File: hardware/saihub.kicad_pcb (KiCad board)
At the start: 2 copper layers, 48 x 28 mm, 55 parts, among them J1 USB4105-GF-A, J2 1x12 2.54mm right-angle, Q1 AO3400A, SW1 BOOT, U1 USBLC6-2SC6, U2 SGM6232YPS8G/TR, U3 ESPC5-32E-H4, U4 TPS2553DBVR, U5 TPS2553DBVR

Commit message: feat(hardware): add header protection and refresh board deliverables
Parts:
- removed R13, R14: 10k, Saihub:R_0603_1608Metric
- added C21: 100n, Saihub:C_0603_1608Metric, F.Cu at (6.00, 4.30)
- added U10: USBLC6-2SC6, Saihub:SOT-23-6, F.Cu at (2.50, 5.50)
- added U6: TPD4E05U06DQAR, Saihub:TPD4E05U06_DQA, F.Cu at (14.5, 4.30)
- added U7: TPD4E05U06DQAR, Saihub:TPD4E05U06_DQA, F.Cu at (22.2, 4.30)
- D3: value SS14 -> SS34
- R10, R12, R9: value 100k -> 10k
- U4, U5: value TPS2553DBVR -> TPS2553DDBVR
- moved Q1 18.0 mm to (2.50, 25.5)
- moved R6 11.2 mm to (2.50, 15.8)
- moved C6 3.30 mm to (2.50, 8.80), turned to 0 degrees
- moved R11 2.36 mm to (15.3, 27.0)
- moved R12 2.05 mm to (22.0, 27.0), turned to 0 degrees
- moved U3 1.95 mm to (14.5, 15.6)
- moved TP3 1.90 mm to (5.60, 27.0)
- moved TP4 1.90 mm to (7.80, 27.0)
- moved TP5 1.90 mm to (10.0, 27.0)
- moved TP6 1.90 mm to (12.2, 27.0)
- moved C13 1.80 mm to (18.5, 27.0)
- moved C8 1.70 mm to (2.50, 14.1), turned to 0 degrees
- moved C7 1.70 mm to (2.50, 10.7), turned to 0 degrees
- moved TP1 0.80 mm to (1.20, 22.3)
- moved TP2 0.80 mm to (3.40, 22.3)
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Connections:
- U3 pad 19: unconnected-(U3-GPIO15-Pad19) -> FAULT4
- U3 pad 5: unconnected-(U3-GPIO3-Pad5) -> FAULT5
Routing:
- net GND: track 225.9 -> 8.61 mm, vias 12 -> 21
- net IO7: track 16.6 -> 42.6 mm, vias 1 -> 3
- net V3V3: track 137.6 -> 115.6 mm, vias 11 -> 13
- net IO3: track 15.1 -> 35.4 mm, vias 1 -> 4
- net FAULT4: track 41.4 -> 60.2 mm, vias 4 -> 6
- net V5: track 76.1 -> 93.4 mm, vias 8 -> 6
- net BUZZ_GATE: track 6.80 -> 23.5 mm, vias 0 -> 2
- net BUZZ_LOW: track 15.1 -> 31.4 mm
- net IO5: track 23.1 -> 38.7 mm, vias 1 -> 2
- net BUZZ_PWM: track 36.9 -> 21.9 mm, vias 4 -> 0
- net FAULT5: track 29.8 -> 43.0 mm, vias 2 -> 4
- net IO4: track 25.6 -> 35.3 mm, vias 1 -> 4
- net IO0: track 21.6 -> 30.8 mm, vias 1 -> 4
- net IO2: track 17.1 -> 25.6 mm, vias 1 -> 0
- net CC2: track 8.73 -> 16.9 mm, vias 2 -> 0
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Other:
- board text added: "SAIHub-Mini Rev A 2026-09-24"
- board text removed: "SAIHub-Mini Rev A 2026-09-18"

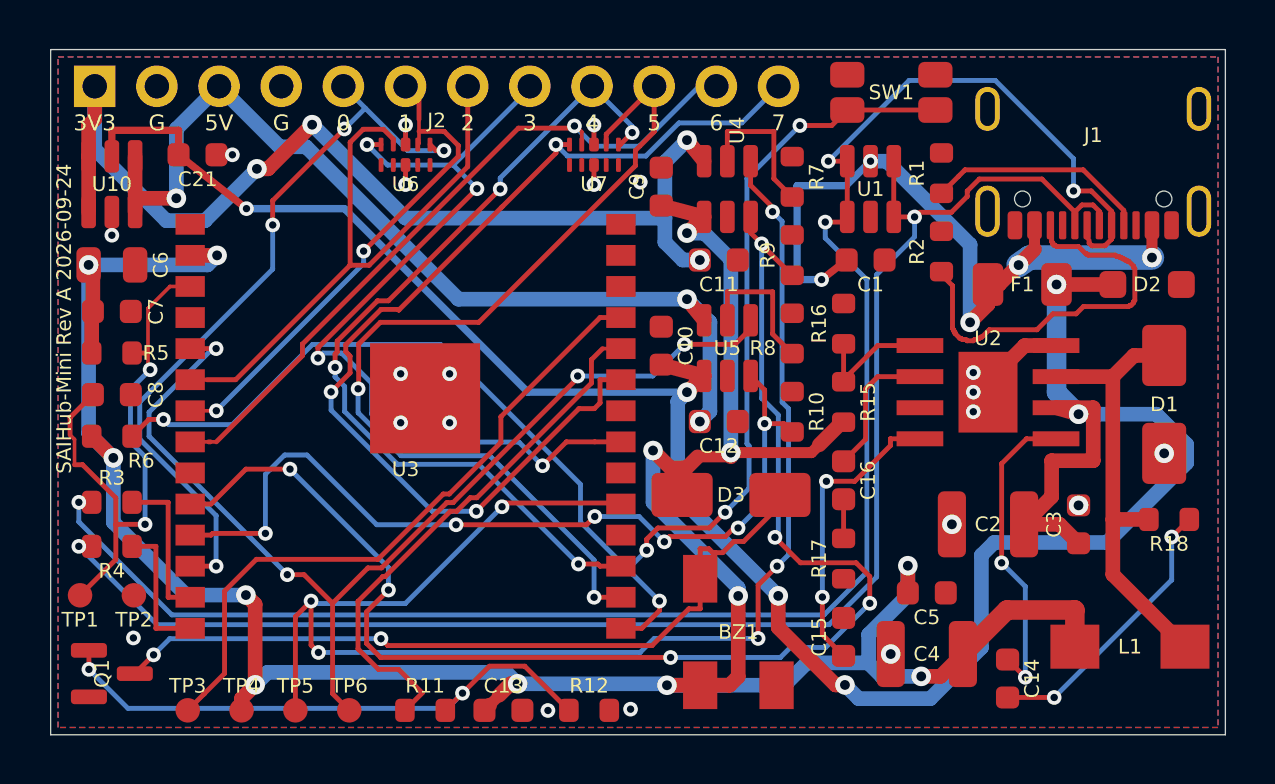
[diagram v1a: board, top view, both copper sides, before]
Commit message: Replace button and add corner antenna module without enlarging PCB
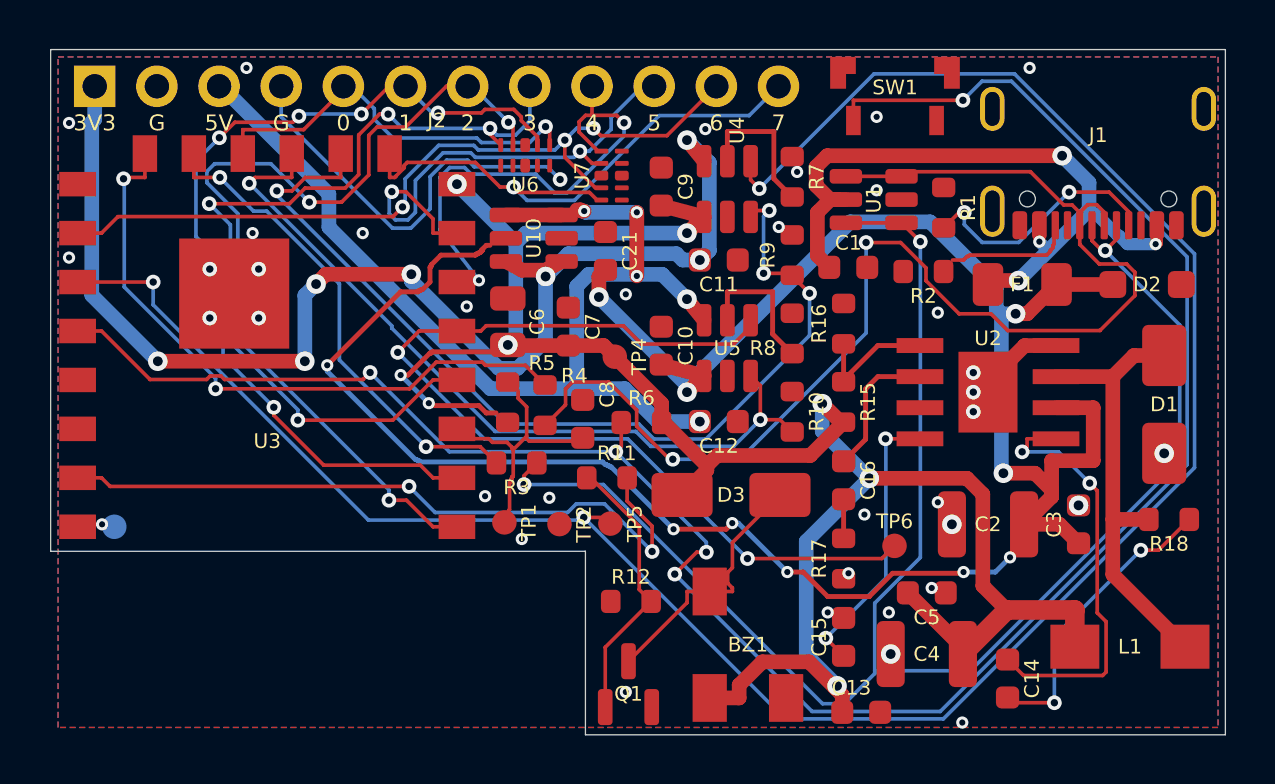
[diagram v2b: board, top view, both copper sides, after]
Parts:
- SW1: footprint Saihub:SW_SPST_EVQP7A -> Saihub:SW_SPST_TS2435VS
- TP3: moved to B.Cu
- U3: value ESPC5-32E-H4 -> ESPC5-12-H4; footprint Saihub:ESPC5-32E-H4 -> Saihub:ESPC5-12-H4
- moved TP6 23.3 mm to (34.5, 20.3)
- moved R6 21.6 mm to (24.1, 15.2), turned to 180 degrees
- moved Q1 21.1 mm to (23.6, 25.9), turned to 90 degrees
- moved TP4 21.0 mm to (23.1, 12.6)
- moved C8 19.3 mm to (21.7, 15.1), turned to 90 degrees
- moved C7 18.7 mm to (21.1, 11.3), turned to 90 degrees
- moved R4 18.6 mm to (20.2, 14.5), turned to 90 degrees
- moved TP2 17.6 mm to (20.8, 19.4)
- moved TP1 17.6 mm to (18.5, 19.3)
- moved U10 17.4 mm to (19.7, 7.71), turned to 180 degrees
- moved C21 17.1 mm to (22.7, 8.23), turned to 90 degrees
- moved R3 16.6 mm to (19.0, 16.9), turned to 180 degrees
- moved C6 16.3 mm to (18.7, 11.1), turned to 90 degrees
- moved R5 16.3 mm to (18.7, 14.4), turned to 90 degrees
- moved TP5 15.0 mm to (22.9, 19.4)
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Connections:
- U3 pad 1: GND -> IO2
- U3 pad 15: BOOT -> GND
- U3 pad 16: IO5 -> IO6
- U3 pad 17: IO4 -> FAULT4
- U3 pad 18: unconnected-(U3-GPIO27-Pad18) -> BOOT
- U3 pad 19: FAULT4 -> unconnected-(U3-GPIO27-Pad19)
- U3 pad 2: V3V3 -> IO1
- U3 pad 21: IO3 -> BUZZ_PWM
- U3 pad 22: unconnected-(U3-NC-Pad22) -> UART_TX
- U3 pad 23: IO7 -> GND
- U3 pad 4: unconnected-(U3-GPIO2-Pad4) -> IO3
- U3 pad 6: IO2 -> IO4
- U3 pad 7: IO1 -> IO5
- U3 pad 8: IO6 -> V3V3
- U3 pad 9: unconnected-(U3-GPIO7-Pad9) -> IO7
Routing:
- net FAULT4: track 60.2 -> 91.9 mm, vias 6 -> 3
- net BOOT: track 58.9 -> 86.7 mm
- net V3V3: track 115.6 -> 88.0 mm, vias 13 -> 8
- net UART_TX: track 26.9 -> 0.25 mm, vias 0 -> 1
- net BUZZ_LOW: track 31.4 -> 10.6 mm, vias 2 -> 0
- net MCU_DP: track 5.72 -> 26.3 mm, vias 0 -> 2
- net IO7: track 42.6 -> 23.6 mm, vias 3 -> 1
- net IO5: track 38.7 -> 20.1 mm
- net PWR3_EN: track 56.6 -> 39.1 mm, vias 6 -> 4
- net IO1: track 20.8 -> 36.9 mm, vias 2 -> 5
- net IO4: track 35.3 -> 20.4 mm, vias 4 -> 2
- net EN: track 23.5 -> 9.00 mm, vias 2 -> 0
- net IO0: track 30.8 -> 16.5 mm, vias 4 -> 1
- net MCU_DM: track 6.25 -> 20.0 mm, vias 0 -> 2
- net CC2: track 16.9 -> 4.71 mm
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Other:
- outline, holes or cut-outs redrawn

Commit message: feat(hardware): add grouped indicators and reproducible routing
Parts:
- added D4: GREEN, Saihub:LED_AA1608, F.Cu at (30.3, 5.20)
- added D5: GREEN, Saihub:LED_AA1608, F.Cu at (30.3, 8.40)
- added D6: RED, Saihub:LED_AA1608, F.Cu at (30.3, 11.6)
- added D7: BLUE, Saihub:LED_AA1608, F.Cu at (30.3, 14.8)
- added R19: 680, Saihub:R_0603_1608Metric, B.Cu at (32.1, 5.20)
- added R20: 1.5k, Saihub:R_0603_1608Metric, B.Cu at (29.2, 8.05)
- added R21: 1.5k, Saihub:R_0603_1608Metric, B.Cu at (32.0, 10.8)
- added R22: 330, Saihub:R_0603_1608Metric, B.Cu at (30.4, 16.6)
- R10, R7, R8, R9: moved to B.Cu
- moved R8 4.31 mm to (26.0, 11.2), turned to 0 degrees
- moved R10 4.00 mm to (34.2, 14.2)
- moved R9 3.96 mm to (34.1, 9.50)
- moved R7 2.47 mm to (28.0, 4.30)
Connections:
- U3 pad 20: unconnected-(U3-GPIO26-Pad20) -> STATUS_LED
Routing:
- net STATUS_LED: track 0.00 -> 32.8 mm, vias 0 -> 3
- net FAULT4: track 91.9 -> 59.3 mm
- net V3_SW: track 52.2 -> 60.4 mm, vias 7 -> 9
- net PWR5_EN: track 32.1 -> 39.9 mm, vias 2 -> 3
- net ILIM4: track 6.10 -> 0.00 mm, vias 0 -> 1
- net BUZZ_LOW: track 10.6 -> 6.37 mm
- net V5: track 94.1 -> 97.6 mm
- net V5_SW: track 43.9 -> 46.2 mm
- net PWR3_EN: track 39.1 -> 41.2 mm, vias 4 -> 5
- net D6_A: track 0.00 -> 1.21 mm, vias 0 -> 1
- net ILIM5: track 5.87 -> 4.74 mm, vias 0 -> 1
- net D4_A: track 0.00 -> 1.10 mm, vias 0 -> 1
- net GND: vias 37 -> 36
- net D7_A: vias 0 -> 1
- net D5_A: vias 0 -> 1

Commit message: fix(hardware): correct assembly footprints and package outlines
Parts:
- BZ1: value KLJ-5020 3.3V -> 5020 3V 4kHz; footprint Saihub:KLJ-5020 -> Saihub:Buzzer_5020_Supplied
- D4, D5, D6, D7: footprint Saihub:LED_AA1608 -> Saihub:LED_0603_1608Metric
- R19: value 680 -> 330
- R20: value 1.5k -> 1.2k
- SW1: footprint Saihub:SW_SPST_TS2435VS -> Saihub:SW_SPST_2X4_LocatingPins
- moved BZ1 0.50 mm to (28.5, 24.8), turned to 0 degrees
- turned D4 to -90 degrees
- turned D5 to -90 degrees
- turned D6 to -90 degrees
- turned D7 to 90 degrees
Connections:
- D4 pad 1: GND -> D4_A
- D4 pad 2: D4_A -> GND
- D5 pad 1: GND -> D5_A
- D5 pad 2: D5_A -> GND
- D6 pad 1: GND -> D6_A
- D6 pad 2: D6_A -> GND
- D7 pad 1: GND -> D7_A
- D7 pad 2: D7_A -> GND
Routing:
- net BUZZ_LOW: track 6.37 -> 11.7 mm
- net V3V3: track 88.0 -> 85.2 mm

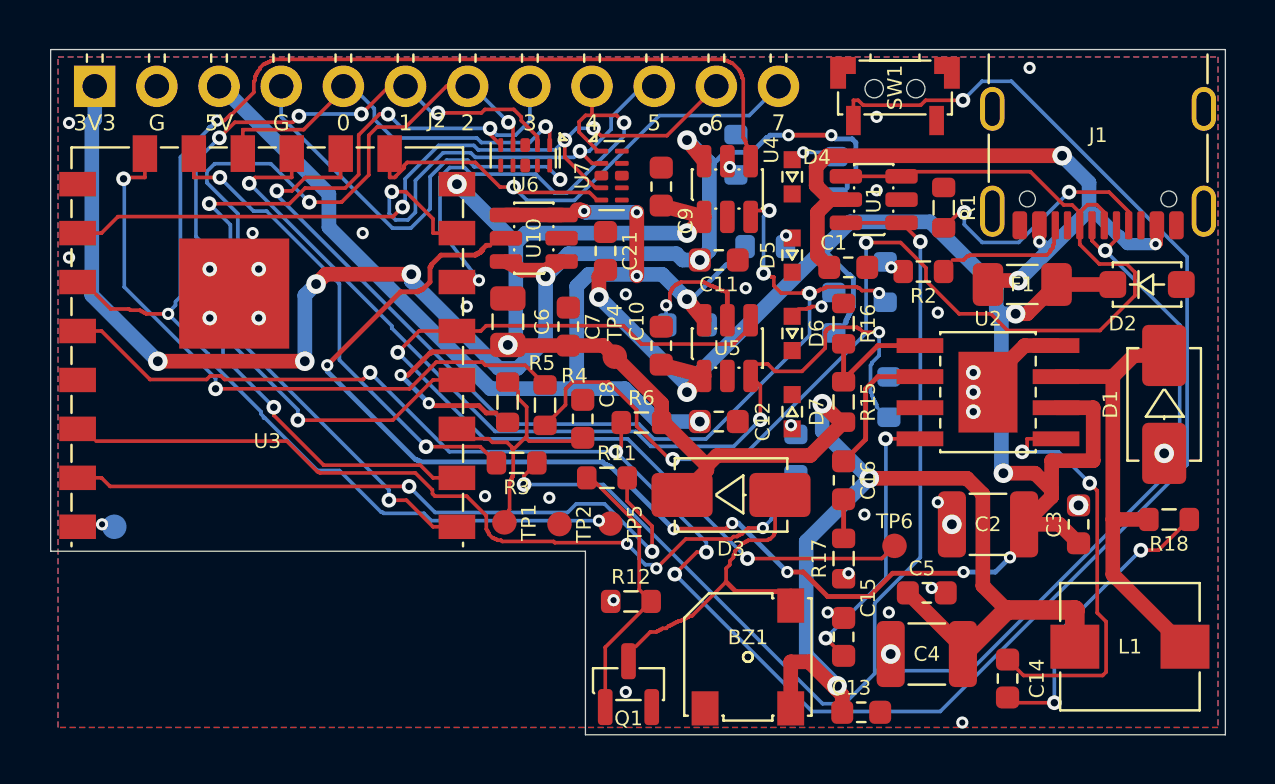
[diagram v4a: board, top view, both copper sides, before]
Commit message: fix(hardware): finish front-only PCB routing and review exports
Place all components and test pads on the front surface while preserving
the shell-critical connector, button, module and indicator positions.
Consolidate the four indicator resistors to 660 ohms, use the smaller
shared protection array at U10, and relocate support parts for local routing.

Complete all signal and ground connections, preserve the supply paths,
and capture replayable copper with the actual pour settings. Refresh the
schematic, interactive BOM, PCB and enclosure review documents.

Validation: zero ERC, DRC, schematic-parity and unconnected findings;
routing reconstruction passes; all six PDF pages visually reviewed.
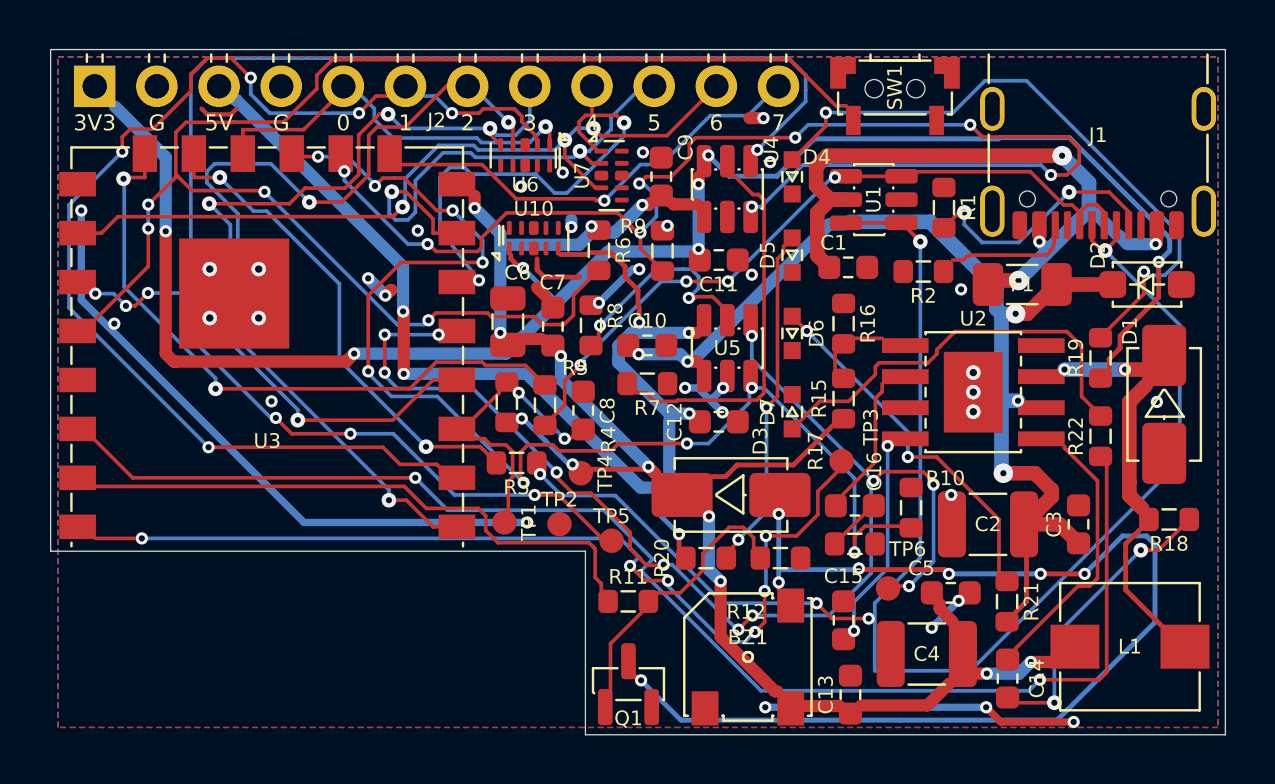
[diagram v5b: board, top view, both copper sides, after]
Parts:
- removed C21: 100n, Saihub:C_0603_1608Metric
- R10, R7, R8, R9, TP3: moved to F.Cu
- R19, R22: value 330 -> 660; moved to F.Cu
- R20: value 1.2k -> 660; moved to F.Cu
- R21: value 1.5k -> 660; moved to F.Cu
- U10: value USBLC6-2SC6 -> TPD4E05U06DQAR; footprint Saihub:SOT-23-6 -> Saihub:TPD4E05U06_DQA
- moved TP3 29.8 mm to (32.3, 16.8)
- moved R21 13.8 mm to (39.1, 22.6)
- moved R19 13.1 mm to (42.9, 12.6)
- moved R20 13.0 mm to (26.8, 20.8)
- moved R22 12.5 mm to (42.9, 15.8)
- moved R7 10.0 mm to (24.4, 13.7), turned to 0 degrees
- moved R9 9.19 mm to (25.0, 8.23)
- moved R6 7.25 mm to (22.4, 8.20), turned to -90 degrees
- moved R12 6.36 mm to (29.8, 20.8), turned to 0 degrees
- moved R11 5.12 mm to (23.6, 22.6), turned to 0 degrees
- moved TP4 4.96 mm to (21.7, 17.3)
- moved R10 4.61 mm to (35.2, 18.7)
- moved R8 3.92 mm to (22.1, 11.3), turned to 90 degrees
- moved TP6 1.76 mm to (34.2, 22.0)
- moved C16 1.14 mm to (32.9, 18.6), turned to 0 degrees
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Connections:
- U10 pad 2: GND -> unconnected-(U10-IO2-Pad2)
- U10 pad 3: V5_SW -> GND
- U10 pad 4: V5_SW -> unconnected-(U10-IO3-Pad4)
- U10 pad 5: V5 -> V5_SW
- U10 pad 6: V3_SW -> unconnected-(U10-NC-Pad6)
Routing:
- net V5: track 97.6 -> 40.5 mm, vias 10 -> 5
- net UART_TX: track 0.25 -> 38.4 mm, vias 1 -> 6
- net V3V3: track 85.2 -> 49.5 mm, vias 8 -> 12
- net BUZZ_LOW: track 11.7 -> 46.0 mm, vias 0 -> 7
- net GND: track 20.6 -> 51.4 mm, vias 36 -> 35
- net BOOT: track 86.8 -> 59.7 mm, vias 5 -> 4
- net D4_A: track 1.10 -> 25.4 mm, vias 1 -> 2
- net USB_DP: track 52.2 -> 28.8 mm, vias 2 -> 4
- net STATUS_LED: track 32.8 -> 55.3 mm, vias 3 -> 2
- net D7_A: track 0.00 -> 16.2 mm, vias 1 -> 0
- net ILIM4: track 0.00 -> 15.0 mm, vias 1 -> 0
- net D5_A: track 0.00 -> 13.2 mm, vias 1 -> 2
- net D6_A: track 1.21 -> 14.2 mm, vias 1 -> 2
- net PWR3_EN: track 41.6 -> 53.3 mm, vias 5 -> 8
- net PWR5_EN: track 40.3 -> 50.1 mm, vias 3 -> 9
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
